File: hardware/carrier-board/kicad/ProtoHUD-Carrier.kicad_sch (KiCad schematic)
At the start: 0 parts

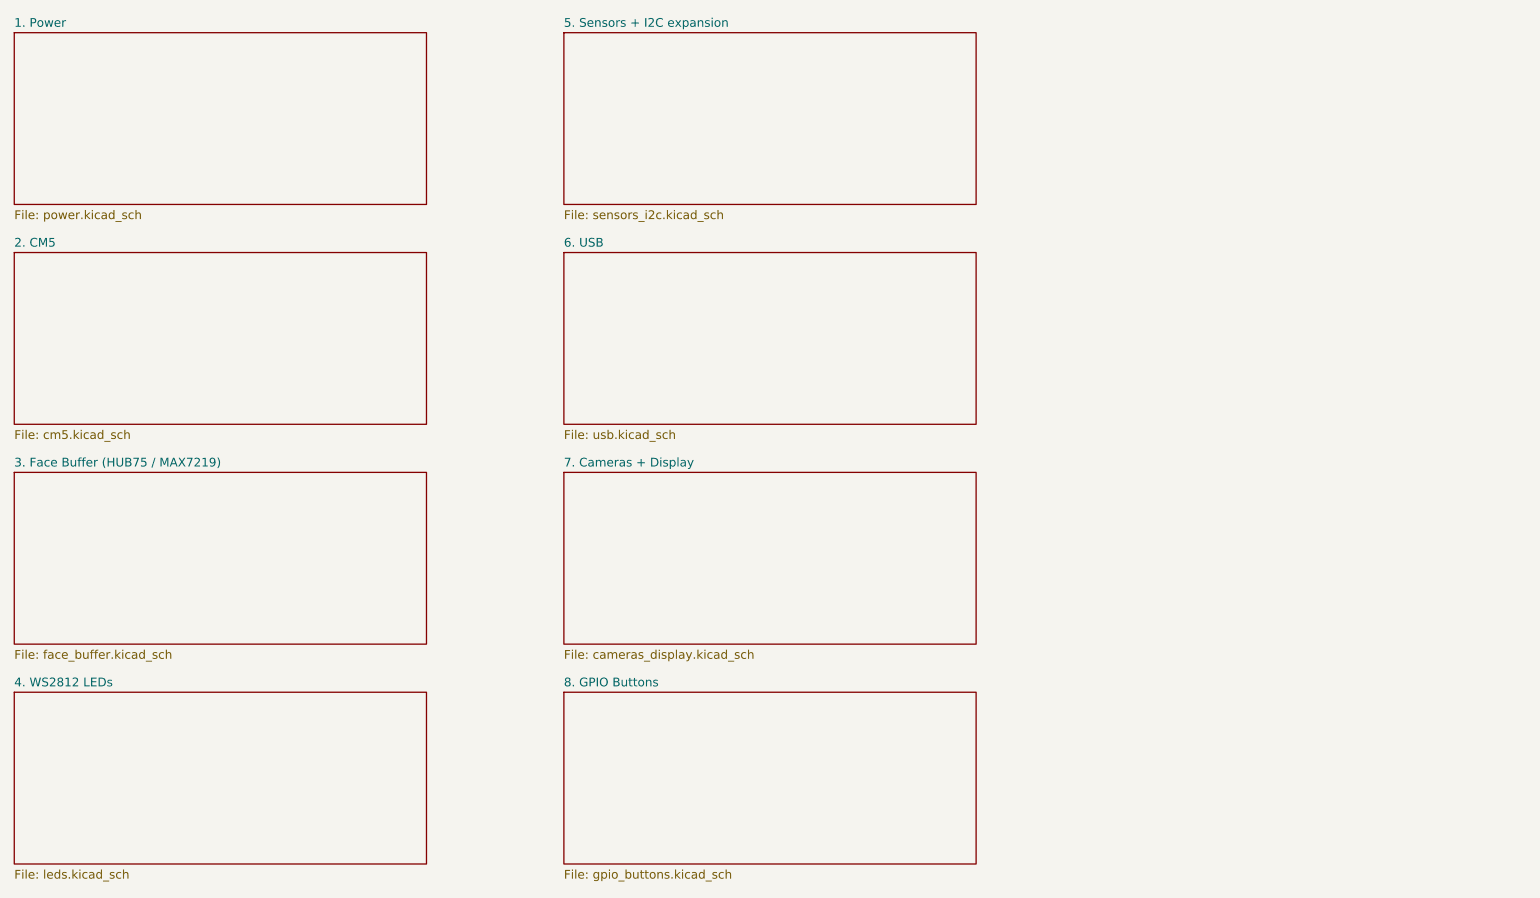
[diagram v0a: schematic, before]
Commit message: Carrier docs + KiCad plan: full two-brain pass (CM5 HUB75 + RP2354B I/O)
Propagate the two-brain architecture across the whole doc set and KiCad plan:
- REQUIREMENTS: restructured M1-M12 (CM5 HUB75; RP2354B core/MAX7219/WS2812/
  sensors/buttons/servos; USB selector + standalone program port); N-list reworked.
- POWER: add +V_SERVO and +3V3_RP rails, servo current budget, updated worked
  total + protection; sensors now on +3V3_RP not CM5 3V3.
- CONNECTORS: J3 re-sourced to RP2354B SPI0, J4 4 WS2812 zones, J5 +SENS_INT,
  J6 BTN1..10, add J12 USB-C, J20-J27 servos, SW1 USB selector, SWD/UART hdrs;
  drop JP1/JP2; fans presented as RP2354B-default-or-CM5 (decision flagged).
- BOM: add RP2354B core, '125/'245 (RP side), USB mux/USB-C/ESD, servo headers,
  +3V3_RP reg; fix '125 double-count and stale HUB75/MAX7219-shared-buffer/JP1.
- MULTI-BACKEND: HUB75+MAX7219 now simultaneous (different brains); firmware
  CompositePanelOutput is the sole remaining blocker.
- IO-EXPANSION: RP2354B is the primary I/O backbone; I2C expanders secondary.
- kicad: 11-sheet plan, stable UUIDs, generator skips populated face_buffer.
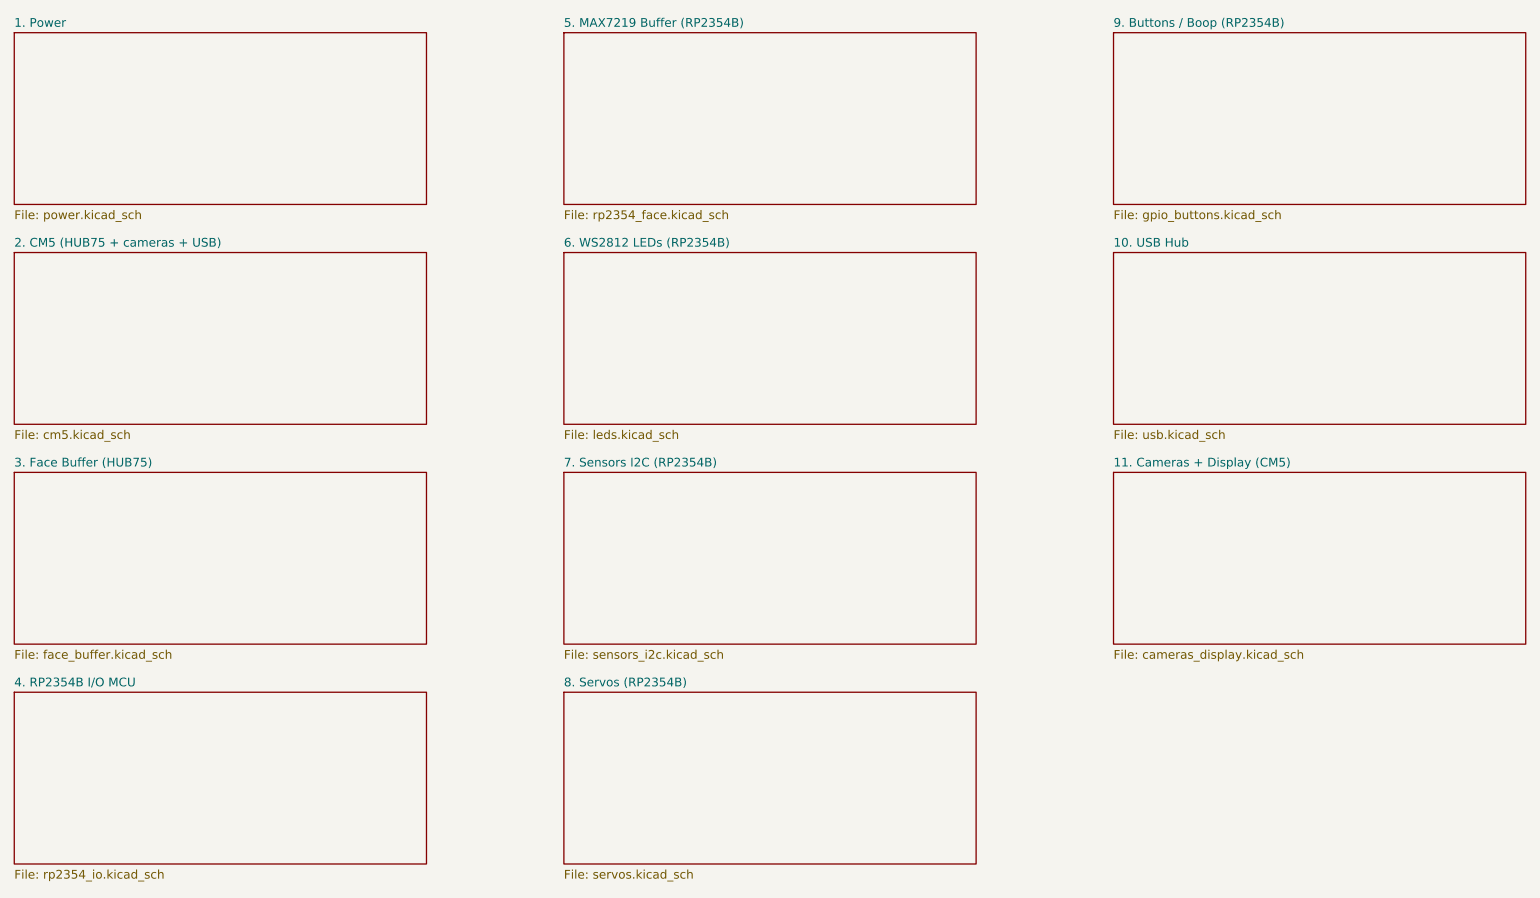
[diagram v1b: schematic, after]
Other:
- sheet 2. CM5 renamed 2. CM5 (HUB75 + cameras + USB)
- sheet 3. Face Buffer (HUB75 / MAX7219) renamed 3. Face Buffer (HUB75)
- sheet 4. WS2812 LEDs renamed 6. WS2812 LEDs (RP2354B)
- sheet 5. Sensors + I2C expansion renamed 7. Sensors I2C (RP2354B)
- sheet 6. USB renamed 10. USB Hub
- sheet 7. Cameras + Display renamed 11. Cameras + Display (CM5)
- sheet 8. GPIO Buttons renamed 9. Buttons / Boop (RP2354B)
- added sheet 4. RP2354B I/O MCU (rp2354_io.kicad_sch)
- added sheet 5. MAX7219 Buffer (RP2354B) (rp2354_face.kicad_sch)
- added sheet 8. Servos (RP2354B) (servos.kicad_sch)
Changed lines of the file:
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@@
   (sheet (at 25.40 57.40) (size 60 25) (fields_autoplaced)
     (stroke (width 0.1524) (type solid)) (fill (color 0 0 0 0.0000))
-    (property "Sheetname" "2. CM5" (at 25.40 56.70 0) (effects (font (size 1.27 1.27)) (justify left bottom)))
+    (property "Sheetname" "2. CM5 (HUB75 + cameras + USB)" (at 25.40 56.70 0) (effects (font (size 1.27 1.27)) (justify left bottom)))
     (property "Sheetfile" "cm5.kicad_sch" (at 25.40 83.20 0) (effects (font (size 1.27 1.27)) (justify left top)))
   )
   (sheet (at 25.40 89.40) (size 60 25) (fields_autoplaced)
     (stroke (width 0.1524) (type solid)) (fill (color 0 0 0 0.0000))
-    (property "Sheetname" "3. Face Buffer (HUB75 / MAX7219)" (at 25.40 88.70 0) (effects (font (size 1.27 1.27)) (justify left bottom)))
+    (property "Sheetname" "3. Face Buffer (HUB75)" (at 25.40 88.70 0) (effects (font (size 1.27 1.27)) (justify left bottom)))
     (property "Sheetfile" "face_buffer.kicad_sch" (at 25.40 115.20 0) (effects (font (size 1.27 1.27)) (justify left top)))
   )
   (sheet (at 25.40 121.40) (size 60 25) (fields_autoplaced)
     (stroke (width 0.1524) (type solid)) (fill (color 0 0 0 0.0000))
-    (property "Sheetname" "4. WS2812 LEDs" (at 25.40 120.70 0) (effects (font (size 1.27 1.27)) (justify left bottom)))
-    (property "Sheetfile" "leds.kicad_sch" (at 25.40 147.20 0) (effects (font (size 1.27 1.27)) (justify left top)))
+    (property "Sheetname" "4. RP2354B I/O MCU" (at 25.40 120.70 0) (effects (font (size 1.27 1.27)) (justify left bottom)))
+    (property "Sheetfile" "rp2354_io.kicad_sch" (at 25.40 147.20 0) (effects (font (size 1.27 1.27)) (justify left top)))
   )
   (sheet (at 105.40 25.40) (size 60 25) (fields_autoplaced)
     (stroke (width 0.1524) (type solid)) (fill (color 0 0 0 0.0000))
-    (property "Sheetname" "5. Sensors + I2C expansion" (at 105.40 24.70 0) (effects (font (size 1.27 1.27)) (justify left bottom)))
-    (property "Sheetfile" "sensors_i2c.kicad_sch" (at 105.40 51.20 0) (effects (font (size 1.27 1.27)) (justify left top)))
+    (property "Sheetname" "5. MAX7219 Buffer (RP2354B)" (at 105.40 24.70 0) (effects (font (size 1.27 1.27)) (justify left bottom)))
+    (property "Sheetfile" "rp2354_face.kicad_sch" (at 105.40 51.20 0) (effects (font (size 1.27 1.27)) (justify left top)))
   )
   (sheet (at 105.40 57.40) (size 60 25) (fields_autoplaced)
     (stroke (width 0.1524) (type solid)) (fill (color 0 0 0 0.0000))
-    (property "Sheetname" "6. USB" (at 105.40 56.70 0) (effects (font (size 1.27 1.27)) (justify left bottom)))
-    (property "Sheetfile" "usb.kicad_sch" (at 105.40 83.20 0) (effects (font (size 1.27 1.27)) (justify left top)))
+    (property "Sheetname" "6. WS2812 LEDs (RP2354B)" (at 105.40 56.70 0) (effects (font (size 1.27 1.27)) (justify left bottom)))
+    (property "Sheetfile" "leds.kicad_sch" (at 105.40 83.20 0) (effects (font (size 1.27 1.27)) (justify left top)))
   )
   (sheet (at 105.40 89.40) (size 60 25) (fields_autoplaced)
     (stroke (width 0.1524) (type solid)) (fill (color 0 0 0 0.0000))
-    (property "Sheetname" "7. Cameras + Display" (at 105.40 88.70 0) (effects (font (size 1.27 1.27)) (justify left bottom)))
-    (property "Sheetfile" "cameras_display.kicad_sch" (at 105.40 115.20 0) (effects (font (size 1.27 1.27)) (justify left top)))
+    (property "Sheetname" "7. Sensors I2C (RP2354B)" (at 105.40 88.70 0) (effects (font (size 1.27 1.27)) (justify left bottom)))
+    (property "Sheetfile" "sensors_i2c.kicad_sch" (at 105.40 115.20 0) (effects (font (size 1.27 1.27)) (justify left top)))
   )
   (sheet (at 105.40 121.40) (size 60 25) (fields_autoplaced)
     (stroke (width 0.1524) (type solid)) (fill (color 0 0 0 0.0000))
-    (property "Sheetname" "8. GPIO Buttons" (at 105.40 120.70 0) (effects (font (size 1.27 1.27)) (justify left bottom)))
-    (property "Sheetfile" "gpio_buttons.kicad_sch" (at 105.40 147.20 0) (effects (font (size 1.27 1.27)) (justify left top)))
+    (property "Sheetname" "8. Servos (RP2354B)" (at 105.40 120.70 0) (effects (font (size 1.27 1.27)) (justify left bottom)))
+    (property "Sheetfile" "servos.kicad_sch" (at 105.40 147.20 0) (effects (font (size 1.27 1.27)) (justify left top)))
+  )
+  (sheet (at 185.40 25.40) (size 60 25) (fields_autoplaced)
+    (stroke (width 0.1524) (type solid)) (fill (color 0 0 0 0.0000))
+    (property "Sheetname" "9. Buttons / Boop (RP2354B)" (at 185.40 24.70 0) (effects (font (size 1.27 1.27)) (justify left bottom)))
+    (property "Sheetfile" "gpio_buttons.kicad_sch" (at 185.40 51.20 0) (effects (font (size 1.27 1.27)) (justify left top)))
+  )
+  (sheet (at 185.40 57.40) (size 60 25) (fields_autoplaced)
+    (stroke (width 0.1524) (type solid)) (fill (color 0 0 0 0.0000))
+    (property "Sheetname" "10. USB Hub" (at 185.40 56.70 0) (effects (font (size 1.27 1.27)) (justify left bottom)))
+    (property "Sheetfile" "usb.kicad_sch" (at 185.40 83.20 0) (effects (font (size 1.27 1.27)) (justify left top)))
+  )
+  (sheet (at 185.40 89.40) (size 60 25) (fields_autoplaced)
+    (stroke (width 0.1524) (type solid)) (fill (color 0 0 0 0.0000))
+    (property "Sheetname" "11. Cameras + Display (CM5)" (at 185.40 88.70 0) (effects (font (size 1.27 1.27)) (justify left bottom)))
+    (property "Sheetfile" "cameras_display.kicad_sch" (at 185.40 115.20 0) (effects (font (size 1.27 1.27)) (justify left top)))
   )
   (sheet_instances
